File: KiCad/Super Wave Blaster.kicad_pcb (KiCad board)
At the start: 2 copper layers, 40 x 21.2 mm, 21 parts, among them J1 EIAJ_Input, J2 PCM5102_I2S, J3 PCM5102_Audio, J4 Power Input, J5 Audio_Jack, J6 Power Input, J7 Audio Out, U1 TLV73333PDBV, U2 CD74HCT14PWR, U3 SN74HC595PWR, U4 SN74LVC8T245PWR

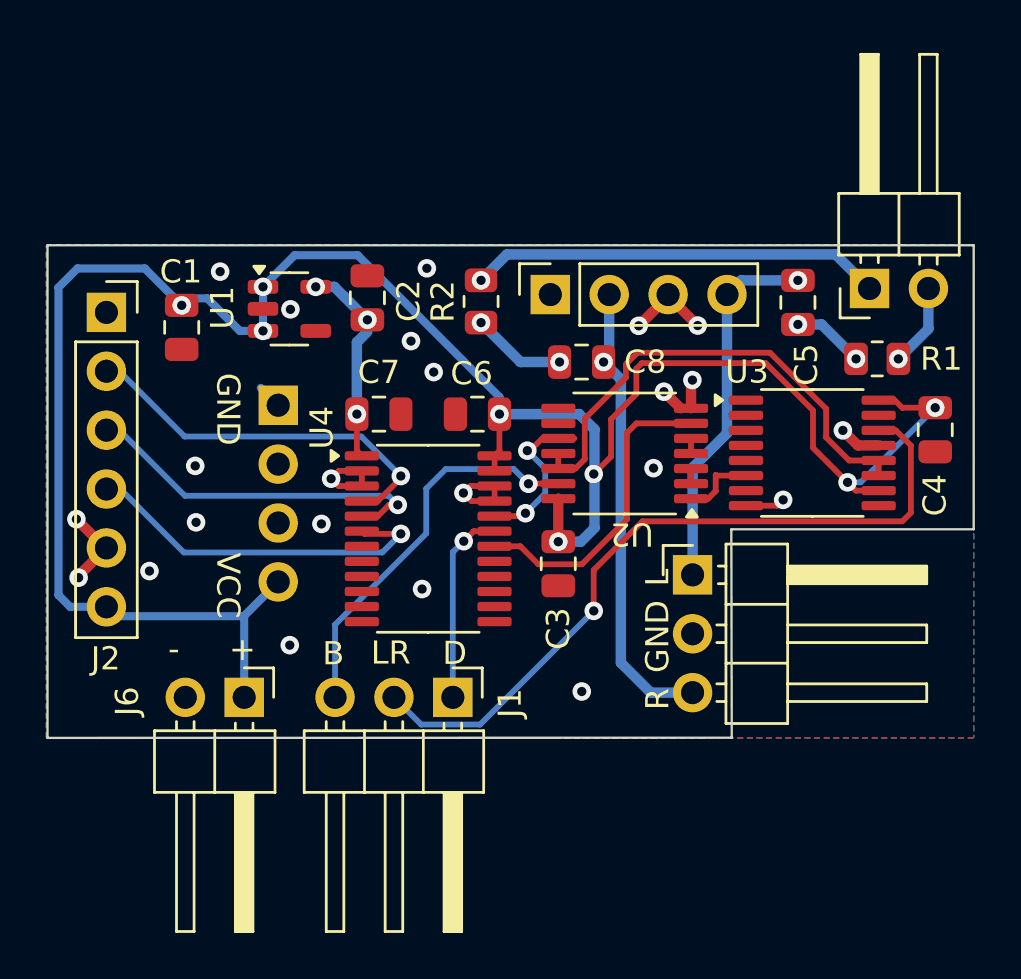
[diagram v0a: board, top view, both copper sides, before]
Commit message: Tighten up traces and ground
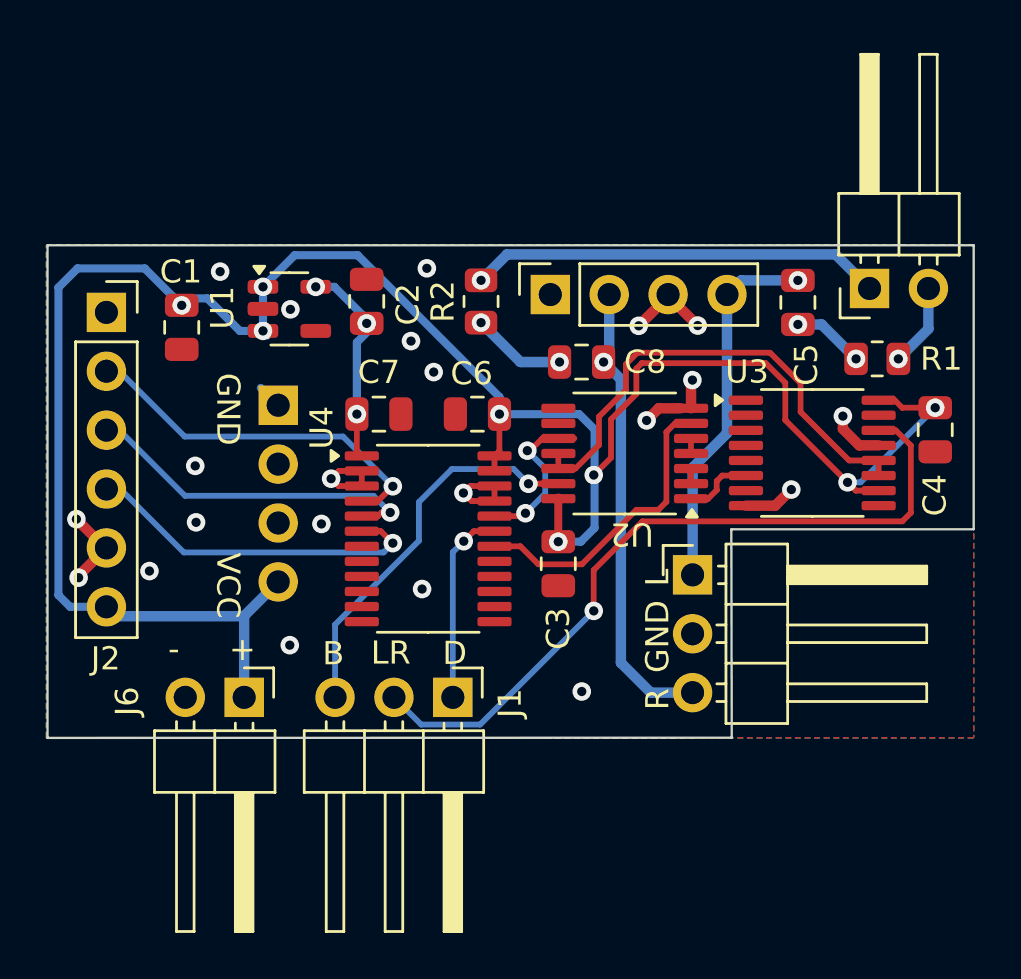
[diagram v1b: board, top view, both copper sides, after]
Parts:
- moved C2 0.16 mm to (128.1, 66.2)
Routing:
- net GND: track 25.1 -> 26.9 mm, vias 23 -> 22
- net BCK_VDD: track 16.8 -> 16.0 mm
- net LRCK_VDD: track 15.9 -> 15.2 mm
- net DIN_VDD: track 15.7 -> 15.0 mm

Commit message: Moved opamp output for better positioning
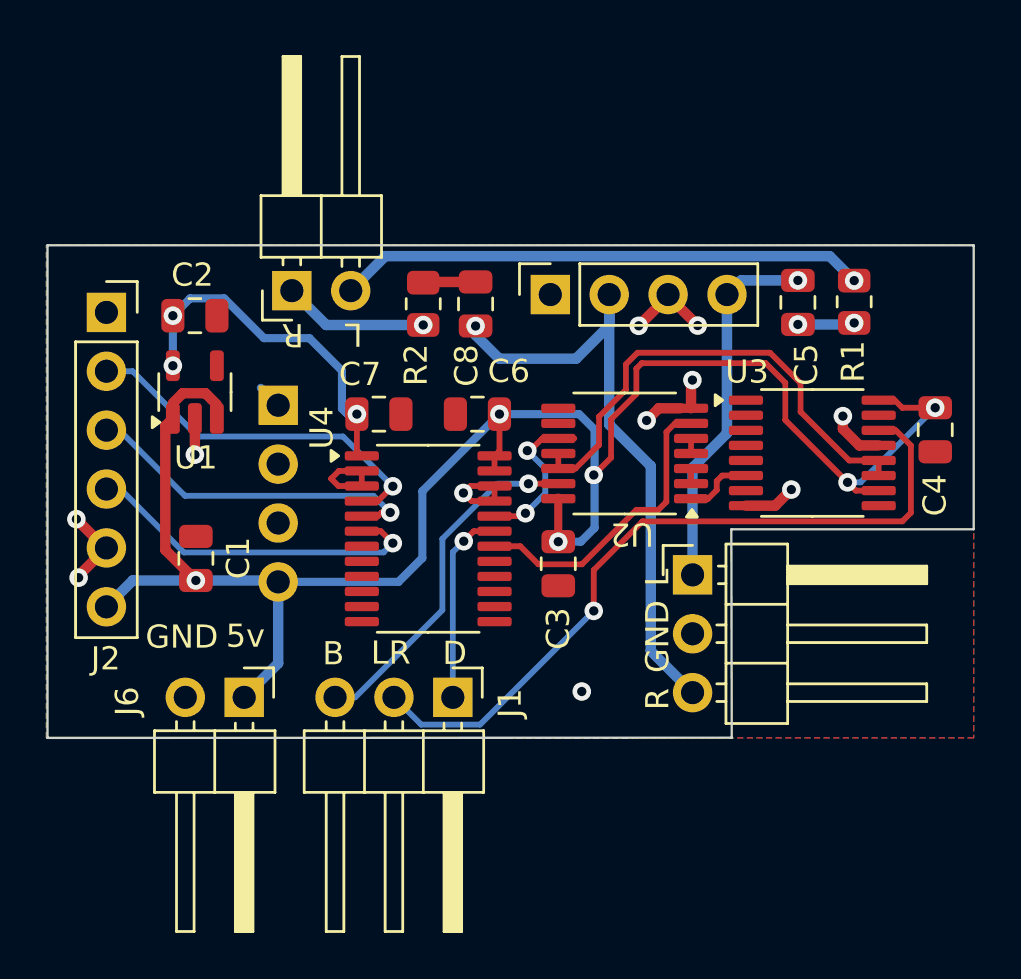
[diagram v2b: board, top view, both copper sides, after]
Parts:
- moved J7 24.9 mm to (124.8, 65.7)
- moved C1 9.99 mm to (120.7, 77.3), turned to 90 degrees
- moved C2 7.44 mm to (120.7, 66.8), turned to 0 degrees
- moved U1 5.43 mm to (120.7, 70.1), turned to 90 degrees
- moved C8 5.21 mm to (132.8, 66.3), turned to 90 degrees
- moved R1 2.66 mm to (149.1, 66.2), turned to 90 degrees
- moved R2 2.50 mm to (130.5, 66.3), turned to -90 degrees
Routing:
- net Net-(J7-Pin_2): track 3.57 -> 22.8 mm
- net VCC: track 96.4 -> 79.8 mm, vias 8 -> 6
- net Net-(J7-Pin_1): track 18.3 -> 6.28 mm
- net AUDIO_R: track 19.9 -> 27.2 mm
- net VDD: track 8.96 -> 15.3 mm
- net Net-(C8-Pad2): track 4.09 -> 2.27 mm, vias 2 -> 0
- net GND: track 26.9 -> 28.5 mm, vias 22 -> 11
- net BCK_EIAJ: track 16.8 -> 15.3 mm
- net Net-(C5-Pad2): track 3.12 -> 2.46 mm
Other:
- board text added: "5v"
- board text added: "V1.11"
- board text removed: "V1.1"
- board text removed: "VCC"

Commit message: Tighten up new layout
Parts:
- moved C4 3.78 mm to (152.3, 67.9), turned to 90 degrees
- moved C5 0.26 mm to (146.9, 66.3)
- moved R1 0.22 mm to (149.3, 66.2)
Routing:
- net VCC: track 79.8 -> 82.0 mm
- net GND: track 28.5 -> 27.6 mm, vias 11 -> 14
- net BCK_INV: track 21.2 -> 21.8 mm
- net LRCK_I2S: track 13.1 -> 12.5 mm
- net BCK_EIAJ: track 15.3 -> 14.7 mm

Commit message: V1.2
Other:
- board text added: "V1.2"
- board text removed: "V1.11"
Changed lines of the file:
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@@
 		)
 	)
-	(gr_text "V1.11"
+	(gr_text "V1.2"
 		(at 153.5 75.5 0)
 		(layer "B.SilkS")

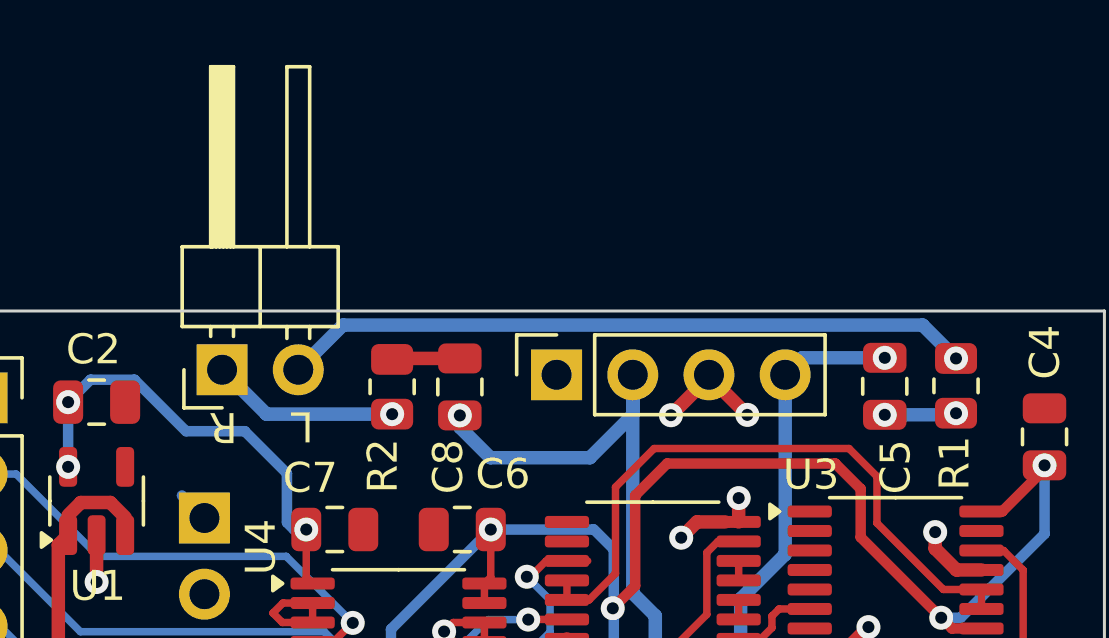
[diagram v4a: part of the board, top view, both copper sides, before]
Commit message: Slight shift opamp out
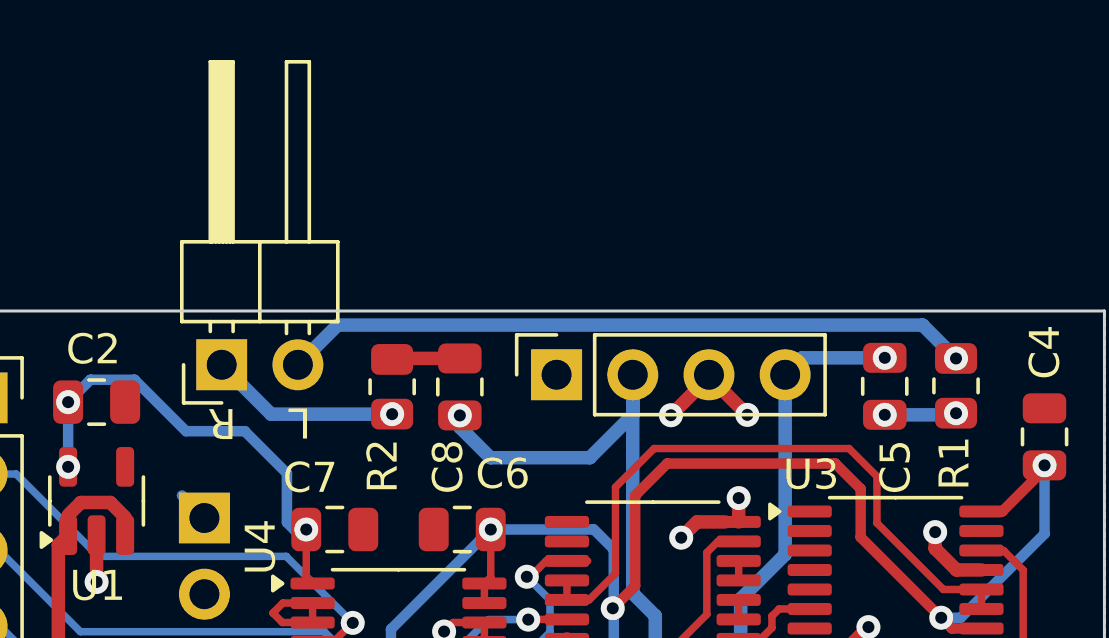
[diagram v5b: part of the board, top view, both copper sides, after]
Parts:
- moved J7 0.17 mm to (124.8, 65.5)
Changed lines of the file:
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@@
 	(footprint "Connector_PinHeader_2.54mm:PinHeader_1x02_P2.54mm_Horizontal"
 		(layer "F.Cu")
-		(at 124.83883 65.708079 90)
+		(at 124.825849 65.543446 90)
 		(descr "Through hole angled pin header, 1x02, 2.54mm pitch, 6mm pin length, single row")
 		(tags "Through hole angled pin header THT 1x02 2.54mm single row")
@@
 	)
 	(gr_text "R"
-		(at 125.353675 67.031235 180)
+		(at 125.31709 66.89709 180)
 		(layer "F.SilkS")
 		(effects
@@
 	)
 	(gr_text "L"
-		(at 127.890234 67.006845 180)
+		(at 127.804869 66.878798 180)
 		(layer "F.SilkS")
 		(effects
@@
 	(segment
 		(start 130.506845 67.188177)
-		(end 126.318928 67.188177)
+		(end 126.47058 67.188177)
 		(width 0.45)
 		(layer "B.Cu")
@@
 	)
 	(segment
-		(start 126.318928 67.188177)
-		(end 124.83883 65.708079)
+		(start 126.47058 67.188177)
+		(end 124.825849 65.543446)
 		(width 0.45)
 		(layer "B.Cu")
@@
 	)
 	(segment
-		(start 148.190532 64.219504)
-		(end 128.867405 64.219504)
+		(start 128.689791 64.219504)
+		(end 127.365849 65.543446)
 		(width 0.45)
 		(layer "B.Cu")
@@
 	)
 	(segment
-		(start 128.867405 64.219504)
-		(end 127.37883 65.708079)
+		(start 148.190532 64.219504)
+		(end 128.689791 64.219504)
 		(width 0.45)
 		(layer "B.Cu")

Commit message: Label cleanup
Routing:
- net Net-(C5-Pad2): track 2.48 -> 2.69 mm, vias 2 -> 0
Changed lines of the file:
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@@
 		(tags "TSSOP SO")
 		(property "Reference" "U4"
-			(at -4.589497 -4.792648 90)
+			(at -4.427526 -2.296886 90)
 			(layer "F.SilkS")
 			(effects
@@
 		(tags "capacitor")
 		(property "Reference" "C1"
-			(at 0.017083 1.829249 90)
+			(at 2.378024 -0.058743 180)
 			(layer "F.SilkS")
 			(effects
@@
 		(net 29)
 	)
-	(via
-		(at 146.928164 67.21099)
-		(size 0.8)
-		(drill 0.4)
-		(layers "F.Cu" "B.Cu")
-		(net 32)
-	)
-	(via
-		(at 149.303718 67.15769)
-		(size 0.8)
-		(drill 0.4)
-		(layers "F.Cu" "B.Cu")
+	(segment
+		(start 149.250418 67.21099)
+		(end 149.303718 67.15769)
+		(width 0.45)
+		(layer "F.Cu")
 		(net 32)
 	)
 	(segment
-		(start 149.117026 67.21099)
-		(end 149.228437 67.099579)
+		(start 146.928164 67.21099)
+		(end 149.250418 67.21099)
 		(width 0.45)
-		(layer "B.Cu")
+		(layer "F.Cu")
 		(net 32)
 	)
 	(segment
-		(start 146.928164 67.21099)
-		(end 149.117026 67.21099)
+		(start 149.117026 67.21099)
+		(end 149.228437 67.099579)
 		(width 0.45)
 		(layer "B.Cu")

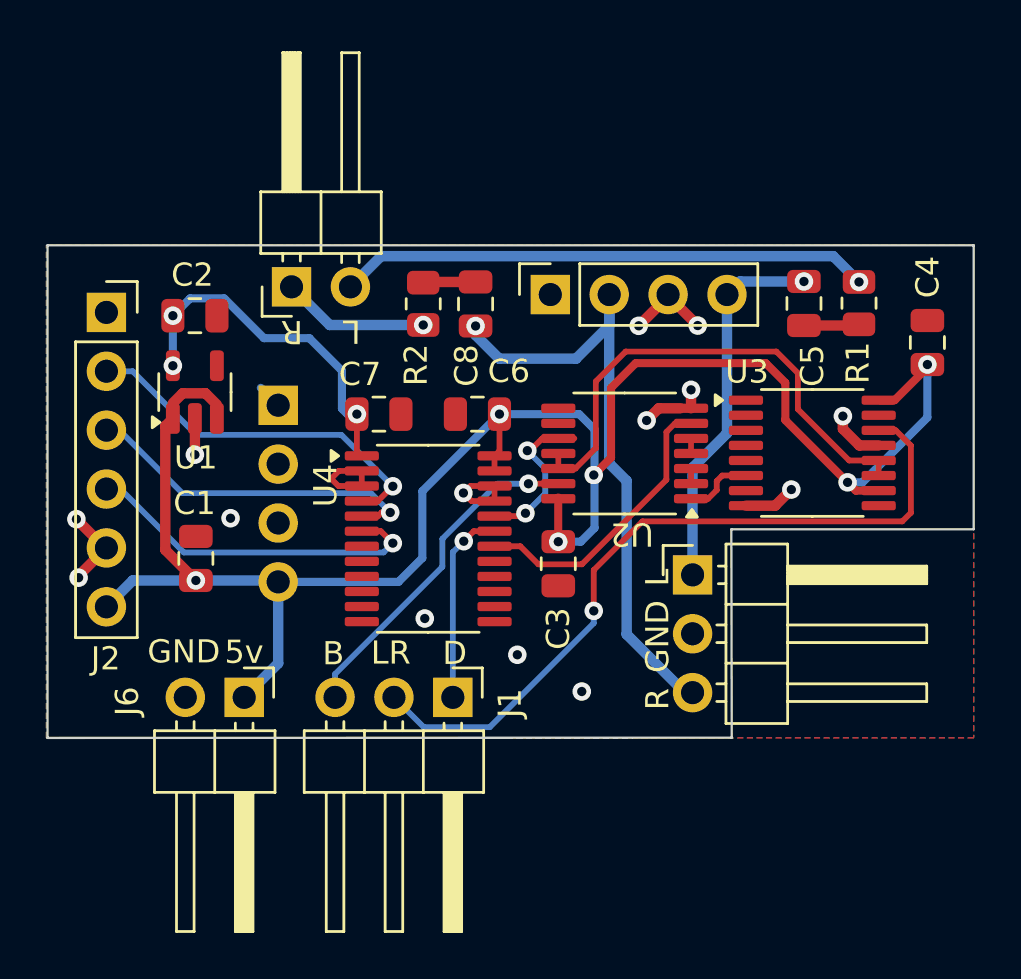
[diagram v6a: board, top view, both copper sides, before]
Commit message: Another layout shift, opamp out moved for more convenient wiring
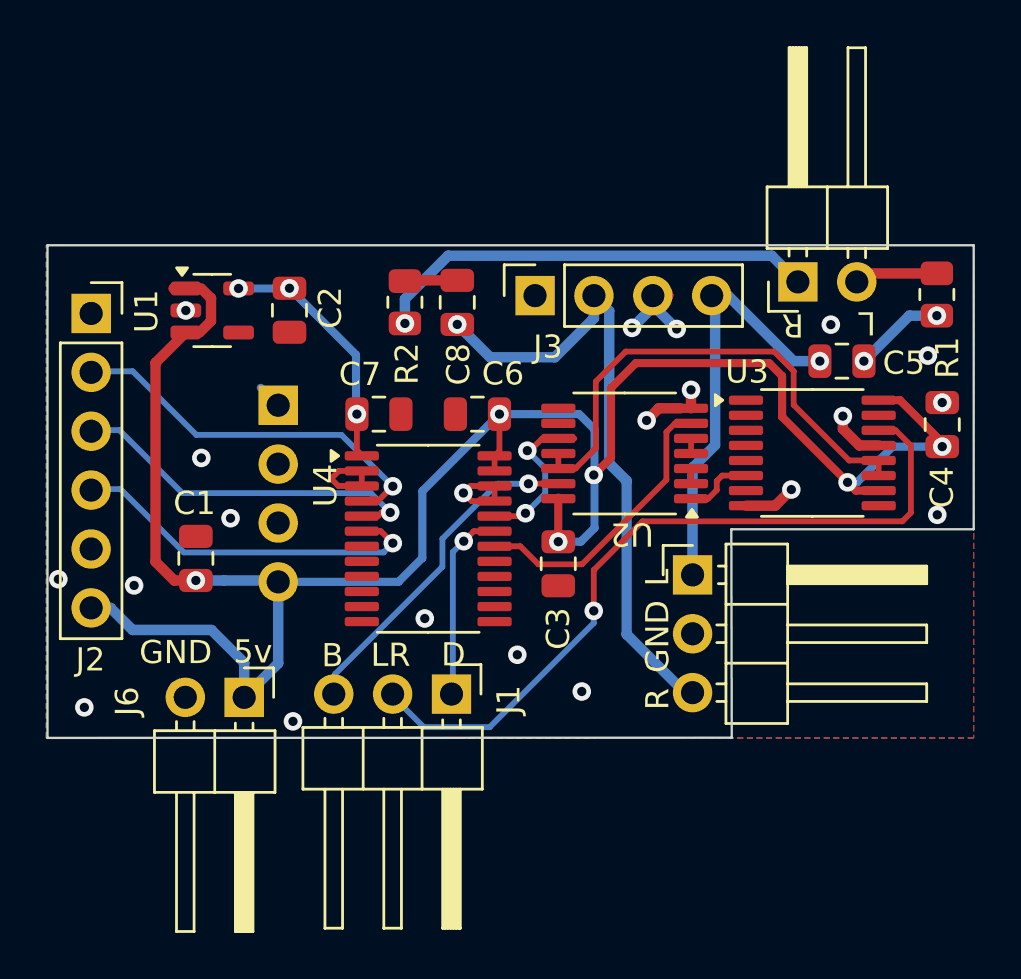
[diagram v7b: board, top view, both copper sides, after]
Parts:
- moved J7 21.8 mm to (146.7, 65.3)
- moved C2 4.09 mm to (124.7, 66.6), turned to -90 degrees
- moved U1 3.60 mm to (121.4, 66.6), turned to 0 degrees
- moved C4 3.60 mm to (152.9, 71.5)
- moved R1 3.38 mm to (152.7, 65.9)
- moved C5 2.98 mm to (148.6, 68.7), turned to 0 degrees
- moved C8 0.79 mm to (132.0, 66.2)
- moved R2 0.79 mm to (129.7, 66.2)
- moved J3 0.66 mm to (135.3, 65.9)
- moved J2 0.66 mm to (116.2, 66.7)
- moved J1 0.15 mm to (131.7, 83.1)
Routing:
- net Net-(J7-Pin_2): track 23.2 -> 3.87 mm, vias 1 -> 0
- net Net-(J7-Pin_1): track 6.36 -> 19.2 mm
- net VCC: track 82.0 -> 90.4 mm
- net VDD: track 15.3 -> 10.7 mm
- net GND: track 27.6 -> 23.2 mm, vias 14 -> 21
- net Net-(C5-Pad2): track 2.69 -> 3.96 mm, vias 0 -> 2
- net AUDIO_L: track 17.3 -> 18.3 mm
